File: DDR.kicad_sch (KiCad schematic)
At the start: 10 parts, among them U2 rv1126/rv1109, U4 W634GU6QB

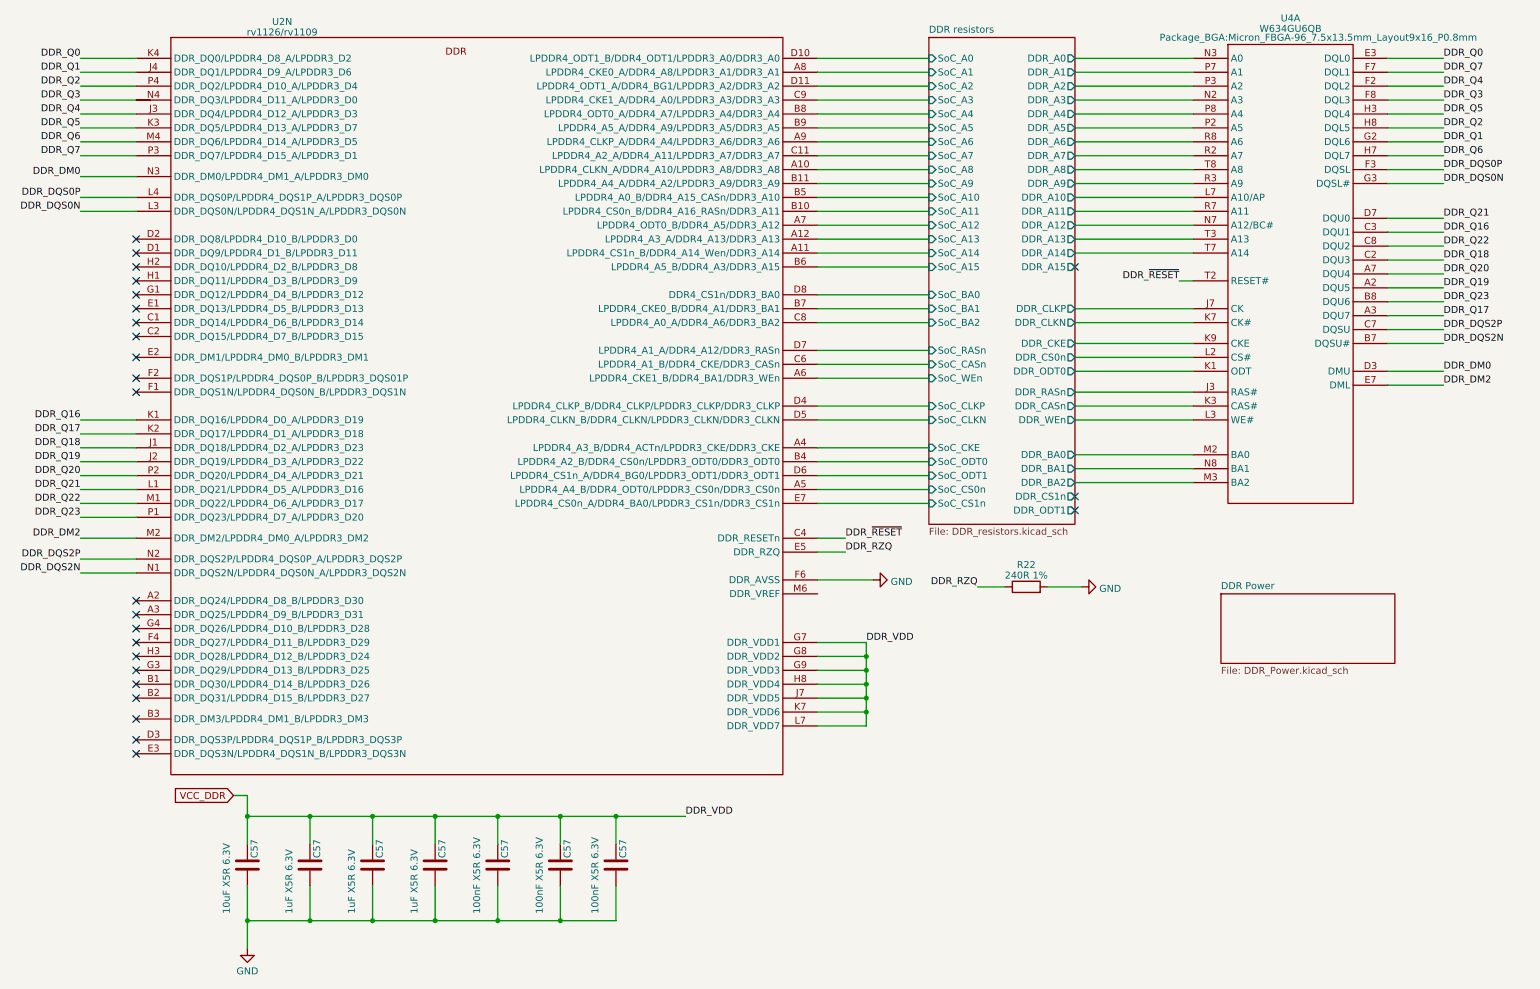
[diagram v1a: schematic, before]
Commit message: replace DDR3 with DDR4
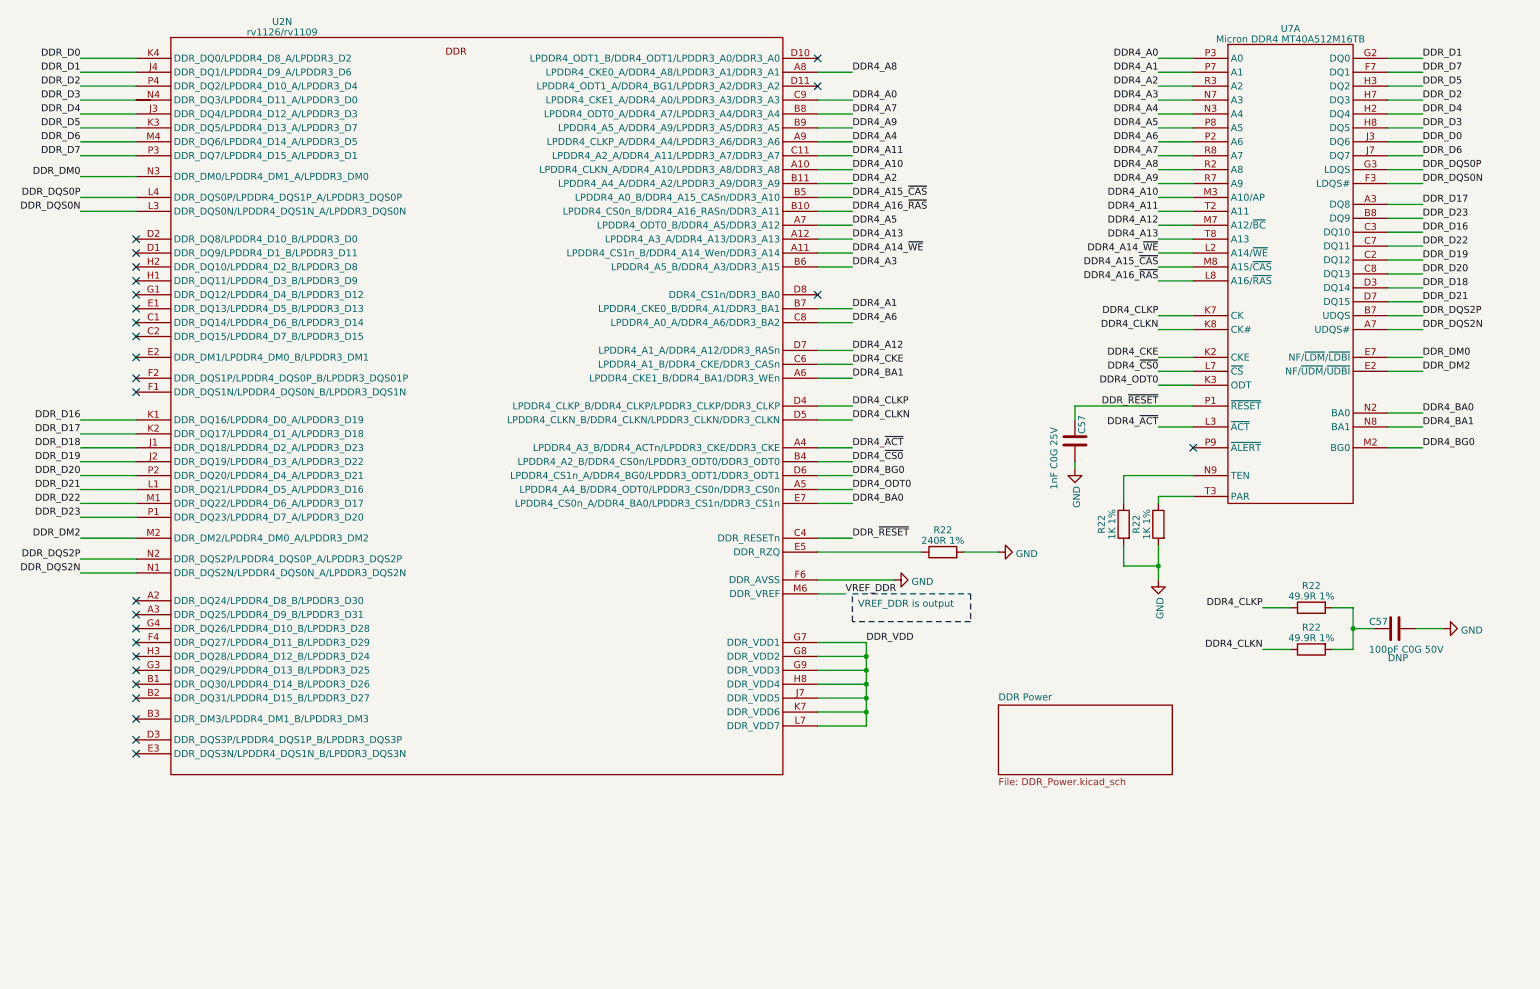
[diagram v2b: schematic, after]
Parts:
- removed C57 (x3): 100nF X5R 6.3V, Capacitor_SMD:C_0201_0603Metric, symbol Device:C
- removed C57 (x3): 1uF X5R 6.3V, Capacitor_SMD:C_0402_1005Metric, symbol Device:C
- removed C57: 10uF X5R 6.3V, Capacitor_SMD:C_0603_1608Metric, symbol Device:C
- removed U4: W634GU6QB, Package_BGA:Micron_FBGA-96_7.5x13.5mm_Layout9x16_P0.8mm, symbol Memory_DDR:W634GU6QB
- added C57: 100pF C0G 50V, Capacitor_SMD:C_0402_1005Metric, symbol Device:C
- added C57: 1nF C0G 25V, Capacitor_SMD:C_0402_1005Metric, symbol Device:C
- added R22 (x2): 1K 1%, Resistor_SMD:R_0402_1005Metric, symbol Device:R
- added R22 (x2): 49.9R 1%, Resistor_SMD:R_0402_1005Metric, symbol Device:R
- added U7: Micron DDR4 MT40A512M16TB, symbol Memory_DDR:Micron_DDR4_MT40A512M16TB
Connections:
- net DDR_DM0: now also U7.E7 (NF/~{LDM}/~{LDBI})
- net DDR_DM2: now also U7.E2 (NF/~{UDM}/~{UDBI})
- net DDR_DQS0N: now also U7.F3 (LDQS#)
- net DDR_DQS0P: now also U7.G3 (LDQS)
- net DDR_DQS2N: now also U7.A7 (UDQS#)
- net DDR_DQS2P: now also U7.B7 (UDQS)
- net DDR_~{RESET}: now also C57.1, U7.P1 (~{RESET})
- net GND: now also C57.2, C57.2, R22.2, R22.2
- net VREF_DDR: now reaches U2.M6 (DDR_VREF)
- net DDR resistors/SoC_A0: no longer names the net of U2.D10 (LPDDR4_ODT1_B/DDR4_ODT1/LPDDR3_A0/DDR3_A0)
- net DDR resistors/SoC_A1 renamed DDR4_A8
- net DDR4_A8: now also U7.R2 (A8)
- net DDR resistors/SoC_A10 renamed DDR4_A15_~{CAS}
- net DDR4_A15_~{CAS}: now also U7.M8 (A15/~{CAS})
- net DDR resistors/SoC_A11 renamed DDR4_A16_~{RAS}
- net DDR4_A16_~{RAS}: now also U7.L8 (A16/~{RAS})
- net DDR resistors/SoC_A12 renamed DDR4_A5
- net DDR4_A5: now also U7.P8 (A5)
- net DDR resistors/SoC_A13 renamed DDR4_A13
- net DDR4_A13: now also U7.T8 (A13)
- net DDR resistors/SoC_A14 renamed DDR4_A14_~{WE}
- net DDR4_A14_~{WE}: now also U7.L2 (A14/~{WE})
- net DDR resistors/SoC_A15 renamed DDR4_A3
- net DDR4_A3: now also U7.N7 (A3)
- net DDR resistors/SoC_A2: no longer names the net of U2.D11 (LPDDR4_ODT1_A/DDR4_BG1/LPDDR3_A2/DDR3_A2)
- net DDR resistors/SoC_A3 renamed DDR4_A0
- net DDR4_A0: now also U7.P3 (A0)
- net DDR resistors/SoC_A4 renamed DDR4_A7
- net DDR4_A7: now also U7.R8 (A7)
- net DDR resistors/SoC_A5 renamed DDR4_A9
- net DDR4_A9: now also U7.R7 (A9)
- net DDR resistors/SoC_A6 renamed DDR4_A4
- net DDR4_A4: now also U7.N3 (A4)
- net DDR resistors/SoC_A7 renamed DDR4_A11
- net DDR4_A11: now also U7.T2 (A11)
- net DDR resistors/SoC_A8 renamed DDR4_A10
- net DDR4_A10: now also U7.M3 (A10/AP)
- net DDR resistors/SoC_A9 renamed DDR4_A2
- net DDR4_A2: now also U7.R3 (A2)
- net DDR resistors/SoC_BA0: no longer names the net of U2.D8 (DDR4_CS1n/DDR3_BA0)
- net DDR resistors/SoC_BA1 renamed DDR4_A1
- net DDR4_A1: now also U7.P7 (A1)
- net DDR resistors/SoC_BA2 renamed DDR4_A6
- net DDR4_A6: now also U7.P2 (A6)
- net DDR resistors/SoC_CASn renamed DDR4_CKE
- net DDR4_CKE: now also U7.K2 (CKE)
- net DDR resistors/SoC_CKE renamed DDR4_~{ACT}
- net DDR4_~{ACT}: now also U7.L3 (~{ACT})
- net DDR resistors/SoC_CLKN renamed DDR4_CLKN
- net DDR4_CLKN: now also R22.1, U7.K8 (CK#)
- net DDR resistors/SoC_CLKP renamed DDR4_CLKP
- net DDR4_CLKP: now also R22.1, U7.K7 (CK)
- net DDR resistors/SoC_CS0n renamed DDR4_ODT0
- net DDR4_ODT0: now also U7.K3 (ODT)
- net DDR resistors/SoC_CS1n renamed DDR4_BA0
- net DDR4_BA0: now also U7.N2 (BA0)
- net DDR resistors/SoC_ODT0 renamed DDR4_~{CS0}
- net DDR4_~{CS0}: now also U7.L7 (~{CS})
- net DDR resistors/SoC_ODT1 renamed DDR4_BG0
- net DDR4_BG0: now also U7.M2 (BG0)
- net DDR resistors/SoC_RASn renamed DDR4_A12
- net DDR4_A12: now also U7.M7 (A12/~{BC})
- net DDR resistors/SoC_WEn renamed DDR4_BA1
- net DDR4_BA1: now also U7.N8 (BA1)
- net DDR_Q0 renamed DDR_D0
- net DDR_D0: now also U7.J3 (DQ6)
- net DDR_Q1 renamed DDR_D1
- net DDR_D1: now also U7.G2 (DQ0)
- net DDR_Q16 renamed DDR_D16
- net DDR_D16: now also U7.C3 (DQ10)
- net DDR_Q17 renamed DDR_D17
- net DDR_D17: now also U7.A3 (DQ8)
- net DDR_Q18 renamed DDR_D18
- net DDR_D18: now also U7.D3 (DQ14)
- net DDR_Q19 renamed DDR_D19
- net DDR_D19: now also U7.C2 (DQ12)
- net DDR_Q2 renamed DDR_D2
- net DDR_D2: now also U7.H7 (DQ3)
- net DDR_Q20 renamed DDR_D20
- net DDR_D20: now also U7.C8 (DQ13)
- net DDR_Q21 renamed DDR_D21
- net DDR_D21: now also U7.D7 (DQ15)
- net DDR_Q22 renamed DDR_D22
- net DDR_D22: now also U7.C7 (DQ11)
- net DDR_Q23 renamed DDR_D23
- net DDR_D23: now also U7.B8 (DQ9)
- net DDR_Q3 renamed DDR_D3
- net DDR_D3: now also U7.H8 (DQ5)
- net DDR_Q4 renamed DDR_D4
- net DDR_D4: now also U7.H2 (DQ4)
- net DDR_Q5 renamed DDR_D5
- net DDR_D5: now also U7.H3 (DQ2)
- net DDR_Q6 renamed DDR_D6
- net DDR_D6: now also U7.J7 (DQ7)
- net DDR_Q7 renamed DDR_D7
- net DDR_D7: now also U7.F7 (DQ1)
- net DDR_RZQ: no longer names the net of R22.1, U2.E5 (DDR_RZQ)
- net VCC_DDR renamed DDR_VDD
- new net: R22.1, U7.N9 (TEN)
- new net: R22.1, U7.T3 (PAR)
- new net: C57.1, R22.2, R22.2
- no-connect marks 25 -> 26
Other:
- removed sheet DDR resistors
- note added: "DNP"
- moved on the sheet: R22

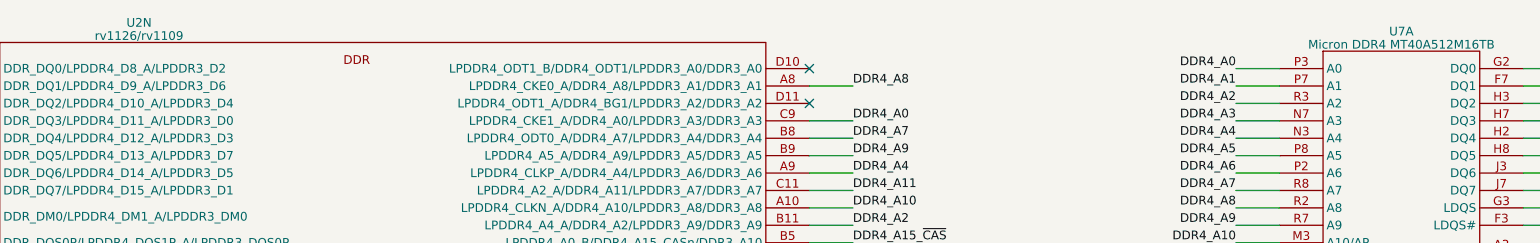
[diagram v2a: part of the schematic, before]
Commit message: updated footprints
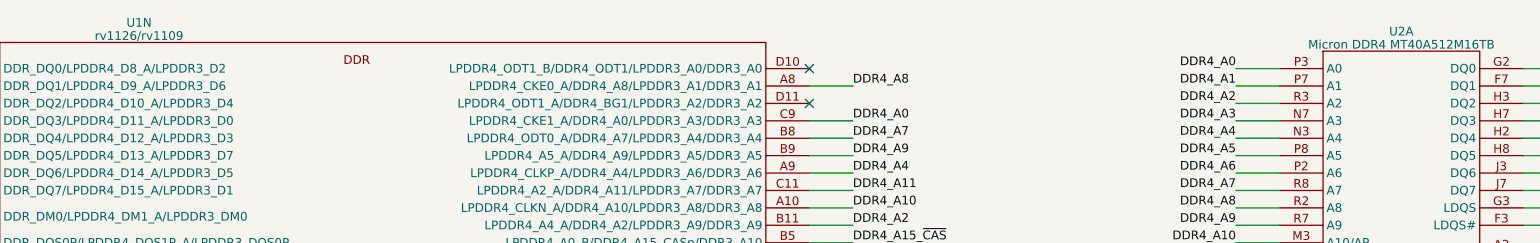
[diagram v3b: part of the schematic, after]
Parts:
- U1: renamed from U2; footprint (none) -> Rockchip_SoC:Rockchip_RV1126_FCCSP409LD_14.0x14.0mm
- renumbered U7 to U2
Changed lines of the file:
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@@
   (symbol (lib_id "Memory_DDR:Micron_DDR4_MT40A512M16TB") (at 245.11 64.77 0) (unit 1)
     (in_bom yes) (on_board yes) (dnp no) (fields_autoplaced)
-    (property "Reference" "U7" (at 245.11 23.7871 0)
+    (property "Reference" "U2" (at 245.11 23.7871 0)
       (effects (font (size 1.27 1.27)))
     )
@@
       (project "leaf"
         (path "/e3b58043-16a3-43c8-9fad-9c9784eebfa4/9453ad46-b3ff-4d4e-8aa6-7cc75aa0f522"
-          (reference "U7") (unit 1)
+          (reference "U2") (unit 1)
         )
       )
@@
         )
         (path "/e3b58043-16a3-43c8-9fad-9c9784eebfa4/9453ad46-b3ff-4d4e-8aa6-7cc75aa0f522"
-          (reference "R27") (unit 1)
+          (reference "R3") (unit 1)
         )
       )
@@
         )
         (path "/e3b58043-16a3-43c8-9fad-9c9784eebfa4/9453ad46-b3ff-4d4e-8aa6-7cc75aa0f522"
-          (reference "C49") (unit 1)
+          (reference "C2") (unit 1)
         )
       )
@@
         )
         (path "/e3b58043-16a3-43c8-9fad-9c9784eebfa4/9453ad46-b3ff-4d4e-8aa6-7cc75aa0f522"
-          (reference "R25") (unit 1)
+          (reference "R4") (unit 1)
         )
       )
@@
         )
         (path "/e3b58043-16a3-43c8-9fad-9c9784eebfa4/9453ad46-b3ff-4d4e-8aa6-7cc75aa0f522"
-          (reference "R26") (unit 1)
+          (reference "R5") (unit 1)
         )
       )
@@
         )
         (path "/e3b58043-16a3-43c8-9fad-9c9784eebfa4/9453ad46-b3ff-4d4e-8aa6-7cc75aa0f522"
-          (reference "C79") (unit 1)
+          (reference "C1") (unit 1)
         )
       )
@@
   (symbol (lib_id "power:GND") (at 191.77 119.38 90) (unit 1)
     (in_bom yes) (on_board yes) (dnp no) (fields_autoplaced)
-    (property "Reference" "#PWR055" (at 198.12 119.38 0)
+    (property "Reference" "#PWR02" (at 198.12 119.38 0)
       (effects (font (size 1.27 1.27)) hide)
     )
@@
       (project "leaf"
         (path "/e3b58043-16a3-43c8-9fad-9c9784eebfa4/9453ad46-b3ff-4d4e-8aa6-7cc75aa0f522"
-          (reference "#PWR055") (unit 1)
+          (reference "#PWR02") (unit 1)
         )
       )
@@
         )
         (path "/e3b58043-16a3-43c8-9fad-9c9784eebfa4/9453ad46-b3ff-4d4e-8aa6-7cc75aa0f522"
-          (reference "R28") (unit 1)
+          (reference "R2") (unit 1)
         )
       )
@@
   (symbol (lib_id "power:GND") (at 172.72 124.46 90) (unit 1)
     (in_bom yes) (on_board yes) (dnp no)
-    (property "Reference" "#PWR057" (at 179.07 124.46 0)
+    (property "Reference" "#PWR01" (at 179.07 124.46 0)
       (effects (font (size 1.27 1.27)) hide)
     )
@@
       (project "leaf"
         (path "/e3b58043-16a3-43c8-9fad-9c9784eebfa4/9453ad46-b3ff-4d4e-8aa6-7cc75aa0f522"
-          (reference "#PWR057") (unit 1)
+          (reference "#PWR01") (unit 1)
         )
       )
@@
         )
         (path "/e3b58043-16a3-43c8-9fad-9c9784eebfa4/9453ad46-b3ff-4d4e-8aa6-7cc75aa0f522"
-          (reference "R32") (unit 1)
+          (reference "R1") (unit 1)
         )
       )
@@
   (symbol (lib_id "power:GND") (at 273.05 133.35 90) (mirror x) (unit 1)
     (in_bom yes) (on_board yes) (dnp no) (fields_autoplaced)
-    (property "Reference" "#PWR064" (at 279.4 133.35 0)
+    (property "Reference" "#PWR05" (at 279.4 133.35 0)
       (effects (font (size 1.27 1.27)) hide)
     )
@@
       (project "leaf"
         (path "/e3b58043-16a3-43c8-9fad-9c9784eebfa4/9453ad46-b3ff-4d4e-8aa6-7cc75aa0f522"
-          (reference "#PWR064") (unit 1)
+          (reference "#PWR05") (unit 1)
         )
       )
@@
   (symbol (lib_id "power:GND") (at 220.98 124.46 0) (mirror y) (unit 1)
     (in_bom yes) (on_board yes) (dnp no) (fields_autoplaced)
-    (property "Reference" "#PWR068" (at 220.98 130.81 0)
+    (property "Reference" "#PWR04" (at 220.98 130.81 0)
       (effects (font (size 1.27 1.27)) hide)
     )
@@
       (project "leaf"
         (path "/e3b58043-16a3-43c8-9fad-9c9784eebfa4/9453ad46-b3ff-4d4e-8aa6-7cc75aa0f522"
-          (reference "#PWR068") (unit 1)
+          (reference "#PWR04") (unit 1)
         )
       )
@@
   (symbol (lib_id "power:GND") (at 205.74 104.14 0) (mirror y) (unit 1)
     (in_bom yes) (on_board yes) (dnp no) (fields_autoplaced)
-    (property "Reference" "#PWR0129" (at 205.74 110.49 0)
+    (property "Reference" "#PWR03" (at 205.74 110.49 0)
       (effects (font (size 1.27 1.27)) hide)
     )
@@
       (project "leaf"
         (path "/e3b58043-16a3-43c8-9fad-9c9784eebfa4/9453ad46-b3ff-4d4e-8aa6-7cc75aa0f522"
-          (reference "#PWR0129") (unit 1)
+          (reference "#PWR03") (unit 1)
         )
       )
@@
   (symbol (lib_id "CPU_Rockchip:rv1126_rv1109") (at 60.96 57.15 0) (unit 14)
     (in_bom yes) (on_board yes) (dnp no) (fields_autoplaced)
-    (property "Reference" "U2" (at 60.96 22.5171 0)
+    (property "Reference" "U1" (at 60.96 22.5171 0)
       (effects (font (size 1.27 1.27)))
     )
@@
       (effects (font (size 1.27 1.27)))
     )
-    (property "Footprint" "" (at 78.74 91.44 0)
+    (property "Footprint" "Rockchip_SoC:Rockchip_RV1126_FCCSP409LD_14.0x14.0mm" (at 78.74 91.44 0)
       (effects (font (size 1.27 1.27)) hide)
     )
@@
       (project "leaf"
         (path "/e3b58043-16a3-43c8-9fad-9c9784eebfa4/9453ad46-b3ff-4d4e-8aa6-7cc75aa0f522"
-          (reference "U2") (unit 14)
-        )
-      )
+          (reference "U1") (unit 14)
+        )
+      )

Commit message: updated Reference, and PCB
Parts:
- added C57 (x3): 100nF X5R 10V, Capacitor_SMD:C_0402_1005Metric, symbol Device:C
- R22: footprint Resistor_SMD:R_0402_1005Metric -> Resistor_SMD:R_0201_0603Metric
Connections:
- net GND: now also C57.1, C57.1, C57.1
- new net VCC_DDR: C57.2, C57.2, C57.2
